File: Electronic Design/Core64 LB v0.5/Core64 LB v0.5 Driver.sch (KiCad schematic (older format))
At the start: 64 parts, among them J11 SSW-116-22-F-S-VS‎, J13 Core Cur. Mon., J14 SSW-116-22-F-S-VS‎, Q10 MMBT4403LT1G, Q11 MMBT4403LT1G, Q12 MMBT4401LT1G, Q13 MMBT4403LT1G, Q14 MMBT4403LT1G, Q15 MMBT4401LT1G, Q16 MMBT4403LT1G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

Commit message: Update 16p to 20p headers for CB
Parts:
- J11, J14: footprint Connector_PinHeader_2.54mm:PinHeader_1x16_P2.54mm_Vertical_SMD_and_TH_Pin1Left -> Connector_PinHeader_2.54mm:PinHeader_1x20_P2.54mm_Vertical; symbol Connector_Generic:Conn_01x16 -> Connector_Generic:Conn_01x20
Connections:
- net labels added: +BATT, 5V0, LED_ARRAY_5V0_SIG, TEENSY_VUSB
- wire segments 222 -> 227
- no-connect marks 0 -> 3
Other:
- note added: "DIGITAL\nLOGIC \nGROUND"
- note removed: "DIGITAL LOGIC GROUND"
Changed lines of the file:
@@
 Wire Wire Line
 	1200 4450 1700 4450
-Text GLabel 2450 1800 0    50   Output ~ 0
+Text GLabel 2550 2000 0    50   Output ~ 0
 XB3
-Text GLabel 2450 1700 0    50   Output ~ 0
+Text GLabel 2550 1900 0    50   Output ~ 0
 XB2
-Text GLabel 2450 1600 0    50   Output ~ 0
+Text GLabel 2550 1800 0    50   Output ~ 0
 XB1
-Text GLabel 2450 1500 0    50   Output ~ 0
+Text GLabel 2550 1700 0    50   Output ~ 0
 XB0
-Text GLabel 2450 1900 0    50   Output ~ 0
+Text GLabel 2550 2100 0    50   Output ~ 0
 XB4
-Text GLabel 2450 2000 0    50   Output ~ 0
+Text GLabel 2550 2200 0    50   Output ~ 0
 XB5
-Text GLabel 2450 2100 0    50   Output ~ 0
+Text GLabel 2550 2300 0    50   Output ~ 0
 XB6
-Text GLabel 2450 2200 0    50   Output ~ 0
+Text GLabel 2550 2400 0    50   Output ~ 0
 XB7
-Text GLabel 2450 1400 0    50   Output ~ 0
+Text GLabel 2550 1600 0    50   Output ~ 0
 XT0,4
-Text GLabel 2450 1300 0    50   Output ~ 0
+Text GLabel 2550 1500 0    50   Output ~ 0
 XT1,5
-Text GLabel 2450 1200 0    50   Output ~ 0
+Text GLabel 2550 1400 0    50   Output ~ 0
 XT2,6
-Text GLabel 2450 1100 0    50   Output ~ 0
+Text GLabel 2550 1300 0    50   Output ~ 0
 XT3,7
 Wire Wire Line
-	2450 1100 2550 1100
-Wire Wire Line
-	2450 1200 2550 1200
-Wire Wire Line
-	2450 1300 2550 1300
-Wire Wire Line
-	2450 1400 2550 1400
-Text GLabel 1400 1200 2    50   Output ~ 0
+	2550 1300 2650 1300
+Wire Wire Line
+	2550 1400 2650 1400
+Wire Wire Line
+	2550 1500 2650 1500
+Wire Wire Line
+	2550 1600 2650 1600
+Text GLabel 1450 1400 2    50   Output ~ 0
 YL1
-Text GLabel 1400 1100 2    50   Output ~ 0
+Text GLabel 1450 1300 2    50   Output ~ 0
 YL0
-Text GLabel 1400 1300 2    50   Output ~ 0
+Text GLabel 1450 1500 2    50   Output ~ 0
 YL2
-Text GLabel 1400 1400 2    50   Output ~ 0
+Text GLabel 1450 1600 2    50   Output ~ 0
 YL3
-Text GLabel 1400 1800 2    50   Output ~ 0
+Text GLabel 1450 2000 2    50   Output ~ 0
 YL7
 Wire Wire Line
-	1350 1500 1350 1700
-Wire Wire Line
-	1350 1700 1400 1700
-Wire Wire Line
-	1400 1100 750  1100
-Wire Wire Line
-	1400 1400 750  1400
-Wire Wire Line
-	1400 1500 1350 1500
-Wire Wire Line
-	1350 1500 750  1500
-Connection ~ 1350 1500
-Wire Wire Line
-	1300 1800 1400 1800
-Wire Wire Line
-	1300 1600 1300 1800
-Wire Wire Line
-	1400 1600 1300 1600
-Wire Wire Line
-	1300 1600 750  1600
-Connection ~ 1300 1600
-Wire Wire Line
-	2450 2200 2550 2200
-Wire Wire Line
-	2450 2100 2550 2100
-$Comp
-L Connector_Generic:Conn_01x16 J14
+	1400 1700 1400 1900
+Wire Wire Line
+	1400 1900 1450 1900
+Wire Wire Line
+	1450 1300 800  1300
+Wire Wire Line
+	1450 1600 800  1600
+Wire Wire Line
+	1450 1700 1400 1700
+Wire Wire Line
+	1400 1700 800  1700
+Connection ~ 1400 1700
+Wire Wire Line
+	1350 2000 1450 2000
+Wire Wire Line
+	1350 1800 1350 2000
+Wire Wire Line
+	1450 1800 1350 1800
+Wire Wire Line
+	1350 1800 800  1800
+Connection ~ 1350 1800
+Wire Wire Line
+	2550 2400 2650 2400
+Wire Wire Line
+	2550 2300 2650 2300
+$Comp
+L Connector_Generic:Conn_01x20 J14
 U 1 1 5E78B5ED
-P 2750 1800
-F 0 "J14" H 1950 2750 50  0000 C CNN
-F 1 "SSW-116-22-F-S-VS‎" H 2350 2650 50  0000 C CNN
-F 2 "Connector_PinHeader_2.54mm:PinHeader_1x16_P2.54mm_Vertical_SMD_and_TH_Pin1Left" H 2750 1800 50  0001 C CNN
-F 3 "~" H 2750 1800 50  0001 C CNN
-	1    2750 1800
-	1    0    0    -1
-$EndComp
-$Comp
-L Connector_Generic:Conn_01x16 J11
+P 2850 2000
+F 0 "J14" H 2050 3150 50  0000 C CNN
+F 1 "SSW-116-22-F-S-VS‎" H 2400 3050 50  0000 C CNN
+F 2 "Connector_PinHeader_2.54mm:PinHeader_1x20_P2.54mm_Vertical" H 2850 2000 50  0001 C CNN
+F 3 "~" H 2850 2000 50  0001 C CNN
+	1    2850 2000
+	1    0    0    -1
+$EndComp
+$Comp
+L Connector_Generic:Conn_01x20 J11
 U 1 1 5E78B5F3
-P 550 1800
-F 0 "J11" H 500 2750 50  0000 C CNN
-F 1 "SSW-116-22-F-S-VS‎" H 100 2650 50  0000 C CNN
-F 2 "Connector_PinHeader_2.54mm:PinHeader_1x16_P2.54mm_Vertical_SMD_and_TH_Pin1Left" H 550 1800 50  0001 C CNN
-F 3 "~" H 550 1800 50  0001 C CNN
-	1    550  1800
+P 600 2000
+F 0 "J11" H 550 3150 50  0000 C CNN
+F 1 "SSW-116-22-F-S-VS‎" H 150 3050 50  0000 C CNN
+F 2 "Connector_PinHeader_2.54mm:PinHeader_1x20_P2.54mm_Vertical" H 600 2000 50  0001 C CNN
+F 3 "~" H 600 2000 50  0001 C CNN
+	1    600  2000
 	-1   0    0    -1
 $EndComp
 Wire Wire Line
-	2450 1800 2550 1800
-Wire Wire Line
-	2450 2000 2550 2000
-Text GLabel 850  1700 2    50   Input ~ 0
+	2550 2000 2650 2000
+Wire Wire Line
+	2550 2200 2650 2200
+Text GLabel 900  1900 2    50   Input ~ 0
 SENSE1
-Text GLabel 850  1800 2    50   Input ~ 0
+Text GLabel 900  2000 2    50   Input ~ 0
 SENSE2
 Wire Wire Line
-	850  1800 750  1800
+	900  2000 800  2000
 $Comp
 L power:GNDD #PWR0148
 U 1 1 5E78B651
-P 1550 2550
-F 0 "#PWR0148" H 1550 2300 50  0001 C CNN
-F 1 "GNDD" H 1554 2395 50  0000 C CNN
-F 2 "" H 1550 2550 50  0001 C CNN
-F 3 "" H 1550 2550 50  0001 C CNN
-	1    1550 2550
-	1    0    0    -1
-$EndComp
-Wire Wire Line
-	1550 2200 1550 2550
-Wire Wire Line
-	750  2100 850  2100
-Wire Wire Line
-	750  2200 1550 2200
-Wire Wire Line
-	800  2400 750  2400
-Wire Wire Line
-	800  2600 750  2600
-Wire Wire Line
-	2550 1500 2450 1500
-Wire Wire Line
-	2550 1600 2450 1600
-Wire Wire Line
-	2550 1700 2450 1700
-Wire Wire Line
-	2550 1900 2450 1900
-Text Notes 800  2850 0    50   ~ 0
-DIGITAL LOGIC GROUND
+P 1400 2750
+F 0 "#PWR0148" H 1400 2500 50  0001 C CNN
+F 1 "GNDD" H 1404 2595 50  0000 C CNN
+F 2 "" H 1400 2750 50  0001 C CNN
+F 3 "" H 1400 2750 50  0001 C CNN
+	1    1400 2750
+	1    0    0    -1
+$EndComp
+Wire Wire Line
+	1400 2400 1400 2750
+Wire Wire Line
+	800  2300 900  2300
+Wire Wire Line
+	800  2400 1400 2400
+Wire Wire Line
+	850  2600 800  2600
+Wire Wire Line
+	850  2800 800  2800
+Wire Wire Line
+	2650 1700 2550 1700
+Wire Wire Line
+	2650 1800 2550 1800
+Wire Wire Line
+	2650 1900 2550 1900
+Wire Wire Line
+	2650 2100 2550 2100
+Text Notes 1250 3200 0    50   ~ 0
+DIGITAL\nLOGIC \nGROUND
 Text Notes 4000 7600 0    50   ~ 0
 SYSTEM POWER GROUND
-Text GLabel 850  2100 2    50   Input ~ 0
+Text GLabel 900  2300 2    50   Input ~ 0
 3V3
 Wire Wire Line
-	750  1200 1400 1200
-Wire Wire Line
-	750  1300 1400 1300
-Wire Wire Line
-	750  1700 850  1700
-Wire Wire Line
-	750  2300 800  2300
-Wire Wire Line
-	750  2500 800  2500
+	800  1400 1450 1400
+Wire Wire Line
+	800  1500 1450 1500
+Wire Wire Line
+	800  1900 900  1900
+Wire Wire Line
+	800  2500 850  2500
+Wire Wire Line
+	800  2700 850  2700
 Text Notes 550  750  0    118  ~ 0
 CORE BOARD INTERCONNECTS
-Text GLabel 850  1900 2    50   BiDi ~ 0
+Text GLabel 900  2100 2    50   BiDi ~ 0
 I2C_CLOCK
-Text GLabel 850  2000 2    50   BiDi ~ 0
+Text GLabel 900  2200 2    50   BiDi ~ 0
 I2C_DATA
-Text GLabel 1400 1700 2    50   Output ~ 0
+Text GLabel 1450 1900 2    50   Output ~ 0
 YL6
-Text GLabel 1400 1600 2    50   Output ~ 0
+Text GLabel 1450 1800 2    50   Output ~ 0
 YL5
-Text GLabel 1400 1500 2    50   Output ~ 0
+Text GLabel 1450 1700 2    50   Output ~ 0
 YL4
 Wire Wire Line
-	750  1900 850  1900
-Wire Wire Line
-	750  2000 850  2000
+	800  2100 900  2100
+Wire Wire Line
+	800  2200 900  2200
 Wire Wire Line
 	4450 6700 4950 6700
@@
 Text Notes 6300 6750 0    50   ~ 0
 All non-polarized capacitors are X7R or X5R ceramic unless otherwise noted.
-Text Notes 1400 2050 0    50   ~ 0
+Text Notes 1450 2250 0    50   ~ 0
 Silkscreen: 3V3 ONLY
-Text GLabel 2450 2300 0    50   Input ~ 0
+Text GLabel 2550 2500 0    50   Input ~ 0
 CP1_EN
-Text GLabel 2450 2400 0    50   Input ~ 0
+Text GLabel 2550 2600 0    50   Input ~ 0
 CP2_EN
-Text GLabel 2450 2500 0    50   Input ~ 0
+Text GLabel 2550 2700 0    50   Input ~ 0
 CP3_EN
-Text GLabel 2450 2600 0    50   Input ~ 0
+Text GLabel 2550 2800 0    50   Input ~ 0
 CP4_EN
-Text GLabel 800  2600 2    50   Input ~ 0
+Text GLabel 850  2800 2    50   Input ~ 0
 CP5_EN
-Text GLabel 800  2500 2    50   Input ~ 0
+Text GLabel 850  2700 2    50   Input ~ 0
 CP6_EN
-Text GLabel 800  2400 2    50   Input ~ 0
+Text GLabel 850  2600 2    50   Input ~ 0
 CP7_EN
-Text GLabel 800  2300 2    50   Input ~ 0
+Text GLabel 850  2500 2    50   Input ~ 0
 CP8_EN
 Wire Wire Line
-	2450 2300 2550 2300
-Wire Wire Line
-	2550 2400 2450 2400
-Wire Wire Line
-	2450 2500 2550 2500
-Wire Wire Line
-	2550 2600 2450 2600
+	2550 2500 2650 2500
+Wire Wire Line
+	2650 2600 2550 2600
+Wire Wire Line
+	2550 2700 2650 2700
+Wire Wire Line
+	2650 2800 2550 2800
 Text Notes 4550 6850 0    50   ~ 0
 D
@@
 	0    1    1    0
 $EndComp
-Text Notes 600  3300 0    79   ~ 0
+Text Notes 2400 7950 0    79   ~ 0
 QxP (PNP) is normally high, low to activate matrix transistor.\nQxN (NPN) is normally low, high to activate matrix transistor.
 Text Notes 3300 6650 0    50   ~ 0
@@
 Text Notes 7950 800  0    50   ~ 0
 Drive Transistor current: 3.3/470=7mA
+NoConn ~ 800  2900
+NoConn ~ 800  3000
+NoConn ~ 800  1200
+$Comp
+L power:+BATT #PWR?
+U 1 1 6036FA36
+P 2050 2900
+AR Path="/5E7548ED/6036FA36" Ref="#PWR?"  Part="1"
+AR Path="/5E755AC8/5D254AE8/6036FA36" Ref="#PWR?"  Part="1"
+AR Path="/5E755AC8/6036FA36" Ref="#PWR0149"  Part="1"
+F 0 "#PWR0149" H 2050 2750 50  0001 C CNN
+F 1 "+BATT" H 2065 3073 50  0000 C CNN
+F 2 "" H 2050 2900 50  0001 C CNN
+F 3 "" H 2050 2900 50  0001 C CNN
+	1    2050 2900
+	1    0    0    -1
+$EndComp
+Wire Wire Line
+	2650 2900 2050 2900
+Text GLabel 2550 3000 0    50   Input ~ 0
+TEENSY_VUSB
+Wire Wire Line
+	2550 3000 2650 3000
+$Comp
+L power:GND #PWR0156
+U 1 1 603C5693
+P 2050 1200
+F 0 "#PWR0156" H 2050 950 50  0001 C CNN
+F 1 "GND" H 2055 1023 50  0000 C CNN
+F 2 "" H 2050 1200 50  0001 C CNN
+F 3 "" H 2050 1200 50  0001 C CNN
+	1    2050 1200
+	1    0    0    -1
+$EndComp
+Wire Wire Line
+	2650 1200 2050 1200
+Text GLabel 2550 1100 0    50   Input ~ 0
+5V0
+Wire Wire Line
+	2550 1100 2650 1100
+Text GLabel 900  1100 2    50   Output ~ 0
+LED_ARRAY_5V0_SIG
+Wire Wire Line
+	800  1100 900  1100
 $EndSCHEMATC

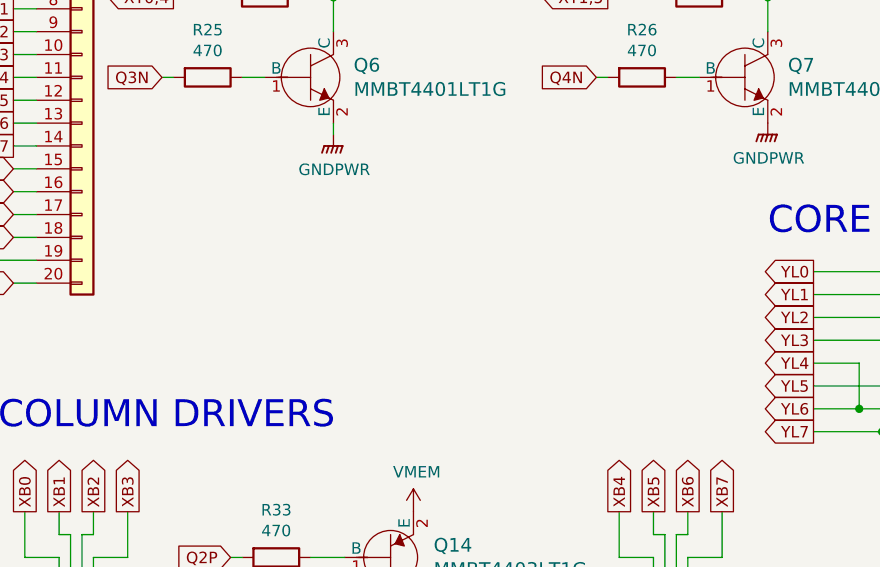
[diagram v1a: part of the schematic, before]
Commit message: LB Layout refinement for optional hall switches
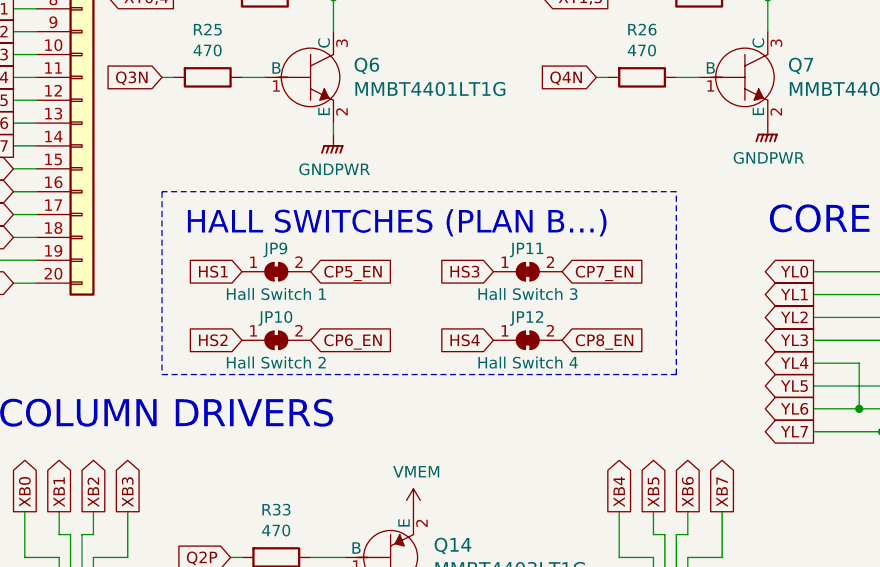
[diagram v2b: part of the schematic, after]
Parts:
- added JP10: Hall Switch 2, Jumper:SolderJumper-2_P1.3mm_Bridged_RoundedPad1.0x1.5mm, symbol Jumper:SolderJumper_2_Bridged
- added JP11: Hall Switch 3, Jumper:SolderJumper-2_P1.3mm_Bridged_RoundedPad1.0x1.5mm, symbol Jumper:SolderJumper_2_Bridged
- added JP12: Hall Switch 4, Jumper:SolderJumper-2_P1.3mm_Bridged_RoundedPad1.0x1.5mm, symbol Jumper:SolderJumper_2_Bridged
- added JP9: Hall Switch 1, Jumper:SolderJumper-2_P1.3mm_Bridged_RoundedPad1.0x1.5mm, symbol Jumper:SolderJumper_2_Bridged
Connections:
- net CP5_EN: now also JP9.2 (B)
- net CP6_EN: now also JP10.2 (B)
- net CP7_EN: now also JP11.2 (B)
- net CP8_EN: now also JP12.2 (B)
- new net HS1: JP9.1 (A)
- new net HS2: JP10.1 (A)
- new net HS3: JP11.1 (A)
- new net HS4: JP12.1 (A)
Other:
- note added: "HALL SWITCHES (PLAN B…)"
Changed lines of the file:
@@
 Wire Wire Line
 	800  1100 900  1100
+Text GLabel 3550 2950 0    50   Input ~ 0
+HS1
+Text GLabel 3550 3250 0    50   Input ~ 0
+HS2
+Text GLabel 4650 2950 0    50   Input ~ 0
+HS3
+Text GLabel 4650 3250 0    50   Input ~ 0
+HS4
+Text GLabel 3850 2950 2    50   Input ~ 0
+CP5_EN
+Text GLabel 3850 3250 2    50   Input ~ 0
+CP6_EN
+Text GLabel 4950 2950 2    50   Input ~ 0
+CP7_EN
+Text GLabel 4950 3250 2    50   Input ~ 0
+CP8_EN
+$Comp
+L Jumper:SolderJumper_2_Bridged JP12
+U 1 1 60397BD0
+P 4800 3250
+F 0 "JP12" H 4800 3150 50  0000 C CNN
+F 1 "Hall Switch 4" H 4800 3350 50  0000 C CNN
+F 2 "Jumper:SolderJumper-2_P1.3mm_Bridged_RoundedPad1.0x1.5mm" H 4800 3250 50  0001 C CNN
+F 3 "~" H 4800 3250 50  0001 C CNN
+	1    4800 3250
+	1    0    0    1
+$EndComp
+$Comp
+L Jumper:SolderJumper_2_Bridged JP11
+U 1 1 603B8476
+P 4800 2950
+F 0 "JP11" H 4800 2850 50  0000 C CNN
+F 1 "Hall Switch 3" H 4800 3050 50  0000 C CNN
+F 2 "Jumper:SolderJumper-2_P1.3mm_Bridged_RoundedPad1.0x1.5mm" H 4800 2950 50  0001 C CNN
+F 3 "~" H 4800 2950 50  0001 C CNN
+	1    4800 2950
+	1    0    0    1
+$EndComp
+$Comp
+L Jumper:SolderJumper_2_Bridged JP9
+U 1 1 6040AAB4
+P 3700 2950
+F 0 "JP9" H 3700 2850 50  0000 C CNN
+F 1 "Hall Switch 1" H 3700 3050 50  0000 C CNN
+F 2 "Jumper:SolderJumper-2_P1.3mm_Bridged_RoundedPad1.0x1.5mm" H 3700 2950 50  0001 C CNN
+F 3 "~" H 3700 2950 50  0001 C CNN
+	1    3700 2950
+	1    0    0    1
+$EndComp
+$Comp
+L Jumper:SolderJumper_2_Bridged JP10
+U 1 1 6041B0A8
+P 3700 3250
+F 0 "JP10" H 3700 3150 50  0000 C CNN
+F 1 "Hall Switch 2" H 3700 3350 50  0000 C CNN
+F 2 "Jumper:SolderJumper-2_P1.3mm_Bridged_RoundedPad1.0x1.5mm" H 3700 3250 50  0001 C CNN
+F 3 "~" H 3700 3250 50  0001 C CNN
+	1    3700 3250
+	1    0    0    1
+$EndComp
+Wire Notes Line
+	3200 3400 5450 3400
+Wire Notes Line
+	5450 3400 5450 2600
+Wire Notes Line
+	5450 2600 3200 2600
+Wire Notes Line
+	3200 2600 3200 3400
+Text Notes 3300 2800 0    98   ~ 0
+HALL SWITCHES (PLAN B…)
 $EndSCHEMATC
